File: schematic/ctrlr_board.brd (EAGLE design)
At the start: 90.5 x 43.2 mm, 31 parts, among them K1 SRLY-19, K2 SRLY-19, K3 SRLY-19, K4 SRLY-19, K5 SRLY-19, K6 SRLY-19

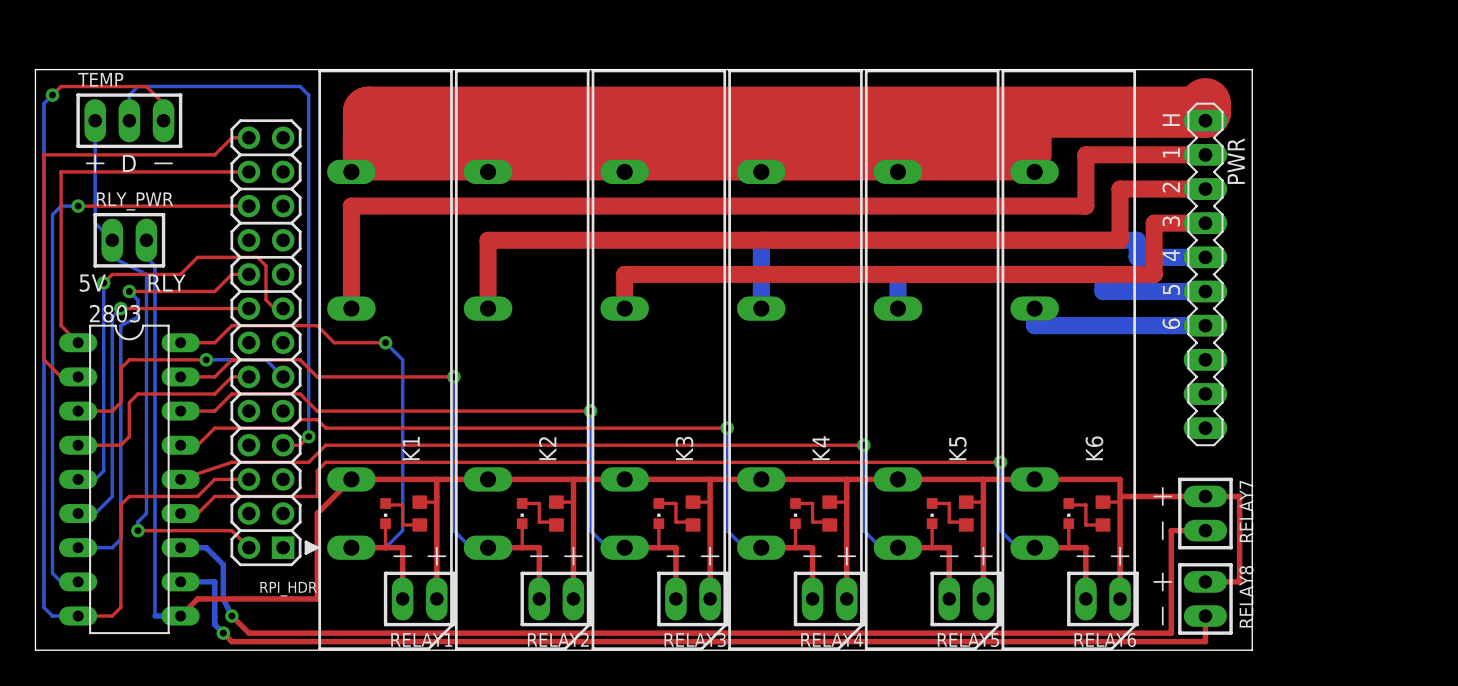
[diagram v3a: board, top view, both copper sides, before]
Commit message: Version 1.1c of expansion board
  * v. 1.1b failed batchpcb DRC (SFE DRC rules were the problem)
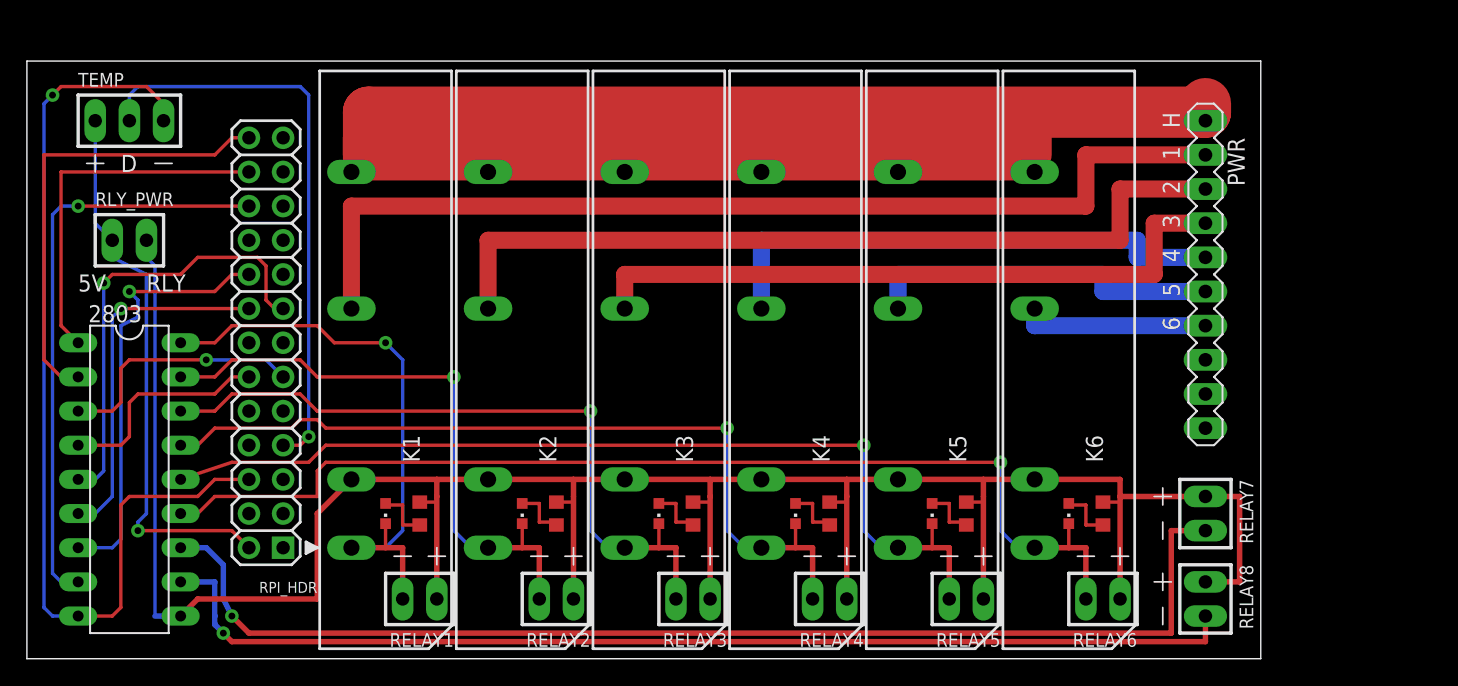
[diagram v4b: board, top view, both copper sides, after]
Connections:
- new net 3.3V: RPI_HDR.1
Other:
- board size 90.5 x 43.2 mm -> 91.7 x 44.4 mm
- board text added: "www.gelberhund.com/relaypi"
- board text removed: "©2012 Doug Zobel www.gelberhund.com"
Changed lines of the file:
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@@
 <board>
 <plain>
-<wire x1="-0.635" y1="-2.54" x2="89.84" y2="-2.54" width="0" layer="20"/>
-<wire x1="89.84" y1="-2.54" x2="89.84" y2="40.63" width="0" layer="20"/>
-<wire x1="89.84" y1="40.63" x2="-0.635" y2="40.63" width="0" layer="20"/>
-<wire x1="-0.635" y1="40.63" x2="-0.635" y2="-2.54" width="0" layer="20"/>
-<text x="22.86" y="39.37" size="1.778" layer="22" rot="MR180">©2012 Doug Zobel  www.gelberhund.com</text>
+<wire x1="-1.27" y1="-3.175" x2="90.475" y2="-3.175" width="0" layer="20"/>
+<wire x1="90.475" y1="-3.175" x2="90.475" y2="41.265" width="0" layer="20"/>
+<wire x1="90.475" y1="41.265" x2="-1.27" y2="41.265" width="0" layer="20"/>
+<wire x1="-1.27" y1="41.265" x2="-1.27" y2="-3.175" width="0" layer="20"/>
+<text x="27.94" y="34.29" size="1.778" layer="22" rot="MR180">www.gelberhund.com/relaypi</text>
 <text x="19.05" y="-1.27" size="1.778" layer="22" rot="MR0">V1.1</text>
-<text x="68.58" y="19.05" size="1.778" layer="22" rot="MR0">Raspberry Pi  Relay Board</text>
+<text x="58.42" y="36.83" size="1.778" layer="22" rot="MR0">Raspberry Pi Relay Board</text>
 </plain>
 <attributes>
@@
 <wire x1="68.58" y1="6.985" x2="68.58" y2="6.77" width="0.254" layer="1"/>
 </signal>
+<signal name="3.3V">
+<contactref element="RPI_HDR" pad="1"/>
+</signal>
 </signals>

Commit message: Board updates for V2.0 hardware
BatchPCB went out of business so switching to oshpark.com.
Removed gerber files since they aren't needed there.  V2.0 has
the following changes:
 * Replace darlington array with 3 WS2801 to do PWM in hardware
 * Add 9th relay output
 * silkscreen high voltage area
 * Add pullup on one wire bus
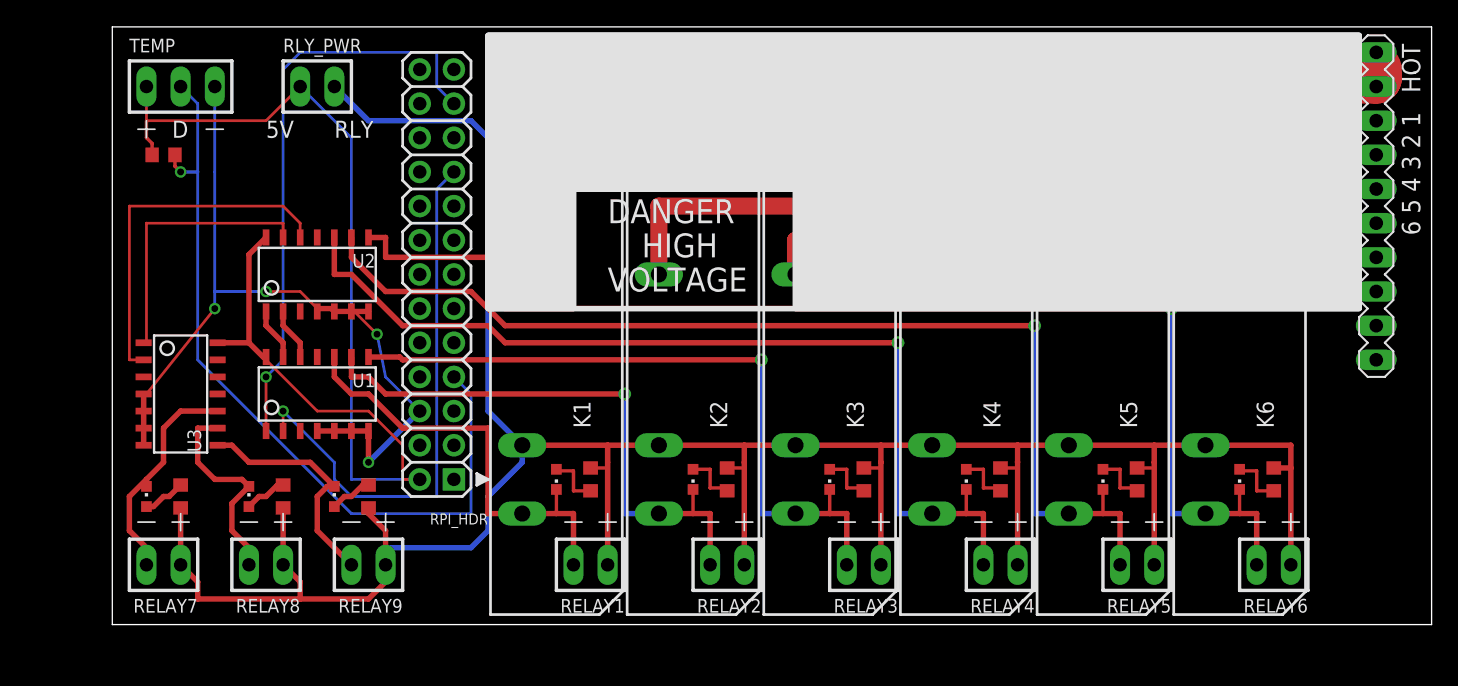
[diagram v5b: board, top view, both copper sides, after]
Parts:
- removed 2803: (no value), uln-udn:DIL18
- removed PWR: 10X1, dz:HDR10
- added .: (no value), dz:HDR10
- added LED7, LED8, LED9: LED, dz:LED0603
- added R10, R7, R8, R9: 330, dz:R0603
- added RELAY9: 2X1+-, dz:HDR2
- added U1, U2, U3: WS2801, SparkFun-DigitalIC:SOP-14
- moved RELAY7 77.6 mm to (8.89, 3.81), turned to 180 degrees
- moved RELAY8 69.9 mm to (16.5, 3.81), turned to 180 degrees
- moved RLY_PWR 18.1 mm to (20.3, 39.4)
- moved RPI_HDR 13.7 mm to (29.2, 25.4)
- moved K1 13.0 mm to (38.1, 21.6)
- moved K3 13.0 mm to (58.4, 21.6)
- moved K6 13.0 mm to (88.9, 21.6)
- moved LED1 13.0 mm to (38.1, 10.2)
- moved LED3 13.0 mm to (58.4, 10.2)
- moved LED6 13.0 mm to (88.9, 10.2)
- moved R3 13.0 mm to (61.0, 10.2)
- moved R4 13.0 mm to (71.1, 10.2)
- moved R5 13.0 mm to (81.3, 10.2)
- moved R6 13.0 mm to (91.4, 10.2)
- moved RELAY3 13.0 mm to (61.0, 3.81)
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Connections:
- new net N$13: LED7.A, R7.1
- new net N$14: LED8.A, R8.1
- new net N$15: U1.13, U2.1
- new net N$16: U1.12, U2.2
- new net N$17: U2.12, U3.2
- new net N$18: U2.13, U3.1
- new net N$19: LED9.A, R9.1
- new net O9: LED9.C, RELAY9.-, U3.8
- new net SPI_CLK: RPI_HDR.23, U1.1
- new net SPI_MISO: RPI_HDR.21
- new net SPI_MOSI: RPI_HDR.19, U1.2
- net 5.0V: now also R10.2, U1.14, U2.14, U3.14
- net GND: now also U1.4, U1.5, U1.6, U1.7, U2.4, U2.5, U2.6, U2.7, U3.4, U3.5, U3.6, U3.7; no longer 2803.9
- net GPIO17: no longer 2803.3
- net GPIO18: no longer 2803.4
- net GPIO22: no longer 2803.5
- net GPIO23: no longer 2803.6
- net GPIO24: no longer 2803.7
- net GPIO25: no longer 2803.8
- net GPIO4: now also R10.1
- net HOT: now also ..1, ..2; no longer PWR.1
- net N$10: now also ..7; no longer PWR.6
- net N$11: now also ..8; no longer PWR.7
- net N$12: now also ..3; no longer PWR.2
- net N$7: now also ..4; no longer PWR.3
- net N$8: now also ..5; no longer PWR.4
- net N$9: now also ..6; no longer PWR.5
- net O1: now also U1.10; no longer 2803.18
- net O2: now also U1.9; no longer 2803.17
- net O3: now also U1.8; no longer 2803.16
- net O4: now also U2.10; no longer 2803.15
- net O5: now also U2.9; no longer 2803.14
- net O6: now also U2.8; no longer 2803.13
- net O7: now also LED7.C, U3.10; no longer 2803.12
- net O8: now also LED8.C, U3.9; no longer 2803.11
- net R_PWR: now also R7.2, R8.2, R9.2, RELAY9.+; no longer 2803.10
- net SPI_CE0: no longer 2803.1
- net SPI_CE1: no longer 2803.2
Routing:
- net O7: track 88.2 -> 16.8 mm, vias 1 -> 0
- net O8: track 81.8 -> 15.5 mm, vias 1 -> 0
- net GPIO25: track 43.7 -> 0.00 mm, vias 1 -> 0
- net SPI_CLK: track 0.00 -> 43.7 mm, vias 0 -> 1
- net 5.0V: track 41.6 -> 82.8 mm, vias 1 -> 0
- net SPI_MOSI: track 0.00 -> 40.9 mm, vias 0 -> 1
- net SPI_CE1: track 34.1 -> 0.00 mm
- net GPIO22: track 33.3 -> 0.00 mm, vias 1 -> 0
- net GPIO24: track 32.3 -> 0.00 mm, vias 1 -> 0
- net SPI_CE0: track 27.2 -> 0.00 mm
- net N$17: track 0.00 -> 27.2 mm
- net GPIO23: track 26.8 -> 0.00 mm, vias 1 -> 0
- net N$18: track 0.00 -> 20.5 mm
- net R_PWR: track 189.1 -> 209.1 mm
- net GPIO17: track 18.8 -> 0.00 mm, vias 1 -> 0
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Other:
- board size 91.7 x 44.4 mm -> 98.1 x 44.4 mm
- board text added: "6 5 4 3 2 1"
- board text added: "DANGER"
- board text added: "HIGH"
- board text added: "HOT"
- board text added: "V2.0"
- board text added: "VOLTAGE"
- board text removed: "V1.1"
